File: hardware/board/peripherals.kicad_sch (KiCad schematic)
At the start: 6 parts, among them U1 RK3568, X1 24 MHz

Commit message: added stuff
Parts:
- added J1: Micro_SD_Card, symbol Connector:Micro_SD_Card
- C1, C2: value 10pF -> 10pF C0G; Class C0G -> (none)
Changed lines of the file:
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@@
 		(dnp no)
 		(property "Reference" "C1"
-			(at 185.42 139.7 0)
+			(at 185.928 140.208 0)
 			(effects
 				(font
@@
 			)
 		)
-		(property "Value" "10pF"
-			(at 185.42 142.24 0)
+		(property "Value" "10pF C0G"
+			(at 186.182 142.24 0)
 			(effects
 				(font
@@
 				)
 				(hide yes)
-			)
-		)
-		(property "Class" "C0G"
-			(at 187.452 144.526 0)
-			(effects
-				(font
-					(size 1.27 1.27)
-				)
 			)
 		)
@@
 			)
 		)
-		(property "Value" "10pF"
+		(property "Value" "10pF C0G"
 			(at 165.1 142.24 0)
 			(effects
@@
 			)
 		)
-		(property "Class" "C0G"
-			(at 163.068 144.526 0)
-			(effects
-				(font
-					(size 1.27 1.27)
-				)
-			)
-		)
 		(pin "2"
 		)
@@
 					(unit 1)
 				)
+			)
+		)
+	)
+	(symbol
+		(lib_id "Connector:Micro_SD_Card")
+		(at 217.17 54.61 0)
+		(unit 1)
+		(exclude_from_sim no)
+		(in_bom yes)
+		(on_board yes)
+		(dnp no)
+		(fields_autoplaced yes)
+		(property "Reference" "J1"
+			(at 217.805 35.56 0)
+			(effects
+				(font
+					(size 1.27 1.27)
+				)
+			)
+		)
+		(property "Value" "Micro_SD_Card"
+			(at 217.805 38.1 0)
+			(effects
+				(font
+					(size 1.27 1.27)
+				)
+			)
+		)
+		(property "Footprint" ""
+			(at 246.38 46.99 0)
+			(effects
+				(font
+					(size 1.27 1.27)
+				)
+				(hide yes)
+			)
+		)
+		(property "Datasheet" "https://www.we-online.com/components/products/datasheet/693072010801.pdf"
+			(at 217.17 54.61 0)
+			(effects
+				(font
+					(size 1.27 1.27)
+				)
+				(hide yes)
+			)
+		)
+		(property "Description" "Micro SD Card Socket"
+			(at 217.17 54.61 0)
+			(effects
+				(font
+					(size 1.27 1.27)
+				)
+				(hide yes)
+			)
+		)
+		(pin "6"
+		)
+		(pin "9"
+		)
+		(pin "3"
+		)
+		(pin "8"
+		)
+		(pin "1"
+		)
+		(pin "4"
+		)
+		(pin "2"
+		)
+		(pin "5"
+		)
+		(pin "7"
+		)
+		(instances
+			(project ""
+				(path "/3bc38516-4fe0-4022-adb8-9fd55b66cd2d/dbcf2505-8053-4a61-9f30-22e0e1eb9f47"
+					(reference "J1")
+					(unit 1)
+				)

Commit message: emmc stuff
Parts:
- U1: LCSC (none) -> C3345225
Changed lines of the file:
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@@
+			)
+		)
+		(property "LCSC" "C3345225"
+			(at 81.28 82.55 0)
+			(effects
+				(font
+					(size 1.27 1.27)
+				)
+				(hide yes)
 			)
 		)

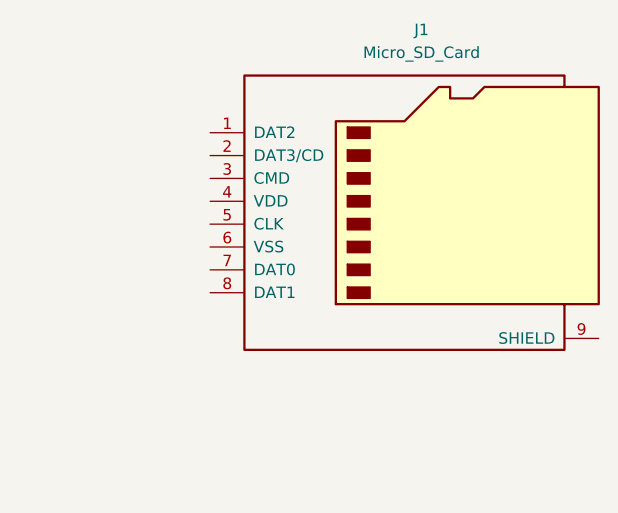
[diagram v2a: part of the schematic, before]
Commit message: MIPI IS FAKE
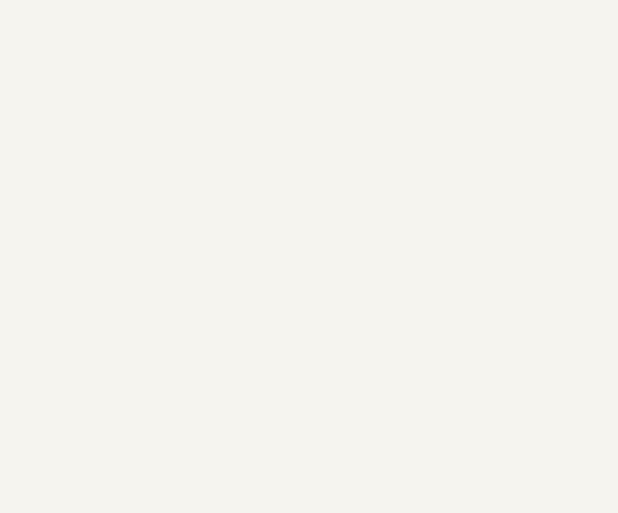
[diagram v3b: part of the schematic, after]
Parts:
- removed J1: Micro_SD_Card, symbol Connector:Micro_SD_Card
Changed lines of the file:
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@@
-		)
-	)
-	(symbol
-		(lib_id "Connector:Micro_SD_Card")
-		(at 217.17 54.61 0)
-		(unit 1)
-		(exclude_from_sim no)
-		(in_bom yes)
-		(on_board yes)
-		(dnp no)
-		(fields_autoplaced yes)
-		(property "Reference" "J1"
-			(at 217.805 35.56 0)
-			(effects
-				(font
-					(size 1.27 1.27)
-				)
-			)
-		)
-		(property "Value" "Micro_SD_Card"
-			(at 217.805 38.1 0)
-			(effects
-				(font
-					(size 1.27 1.27)
-				)
-			)
-		)
-		(property "Footprint" ""
-			(at 246.38 46.99 0)
-			(effects
-				(font
-					(size 1.27 1.27)
-				)
-				(hide yes)
-			)
-		)
-		(property "Datasheet" "https://www.we-online.com/components/products/datasheet/693072010801.pdf"
-			(at 217.17 54.61 0)
-			(effects
-				(font
-					(size 1.27 1.27)
-				)
-				(hide yes)
-			)
-		)
-		(property "Description" "Micro SD Card Socket"
-			(at 217.17 54.61 0)
-			(effects
-				(font
-					(size 1.27 1.27)
-				)
-				(hide yes)
-			)
-		)
-		(pin "6"
-		)
-		(pin "9"
-		)
-		(pin "3"
-		)
-		(pin "8"
-		)
-		(pin "1"
-		)
-		(pin "4"
-		)
-		(pin "2"
-		)
-		(pin "5"
-		)
-		(pin "7"
-		)
-		(instances
-			(project ""
-				(path "/3bc38516-4fe0-4022-adb8-9fd55b66cd2d/dbcf2505-8053-4a61-9f30-22e0e1eb9f47"
-					(reference "J1")
-					(unit 1)
-				)
-			)
 		)
 	)

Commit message: aaa
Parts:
- added C198: 1uF X5R 10V, Capacitor_SMD:C_0402_1005Metric, symbol Device:C
- added C199: 10pF C0G 50V, Capacitor_SMD:C_0402_1005Metric, symbol Device:C
- added CN1: PJ-393 8PJ, lcsc:AUDIO-SMD_PJ-393-8PJ, symbol lcsc:PJ-3938PJ
- added R129: 100R 5%, Resistor_SMD:R_0402_1005Metric, symbol Device:R
- added R139: 2.2K 5%, Resistor_SMD:R_0402_1005Metric, symbol Device:R
- added R140, R141: 0R 5%, Resistor_SMD:R_0402_1005Metric, symbol Device:R
- added U46, U48: ESD5451N_C5261080, lcsc:DFN1006-2L-BI, symbol lcsc:ESD5451N_C5261080
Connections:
- net GND: now also C198.2, C199.2, U46.1, U48.1
- new net: CN1.1, CN1.5, R140.1, U48.2
- new net: C198.1, R129.1, R139.2
- new net: CN1.2, CN1.6, R141.1
- new net: CN1.3, CN1.7
- new net: CN1.4, CN1.8
- new net HPL_OUT: R140.2
- new net HPR_OUT: R141.2
- new net MIC1_INP: C199.1, R139.1, U46.2
- new net VCCIO_ACODEC: R129.2

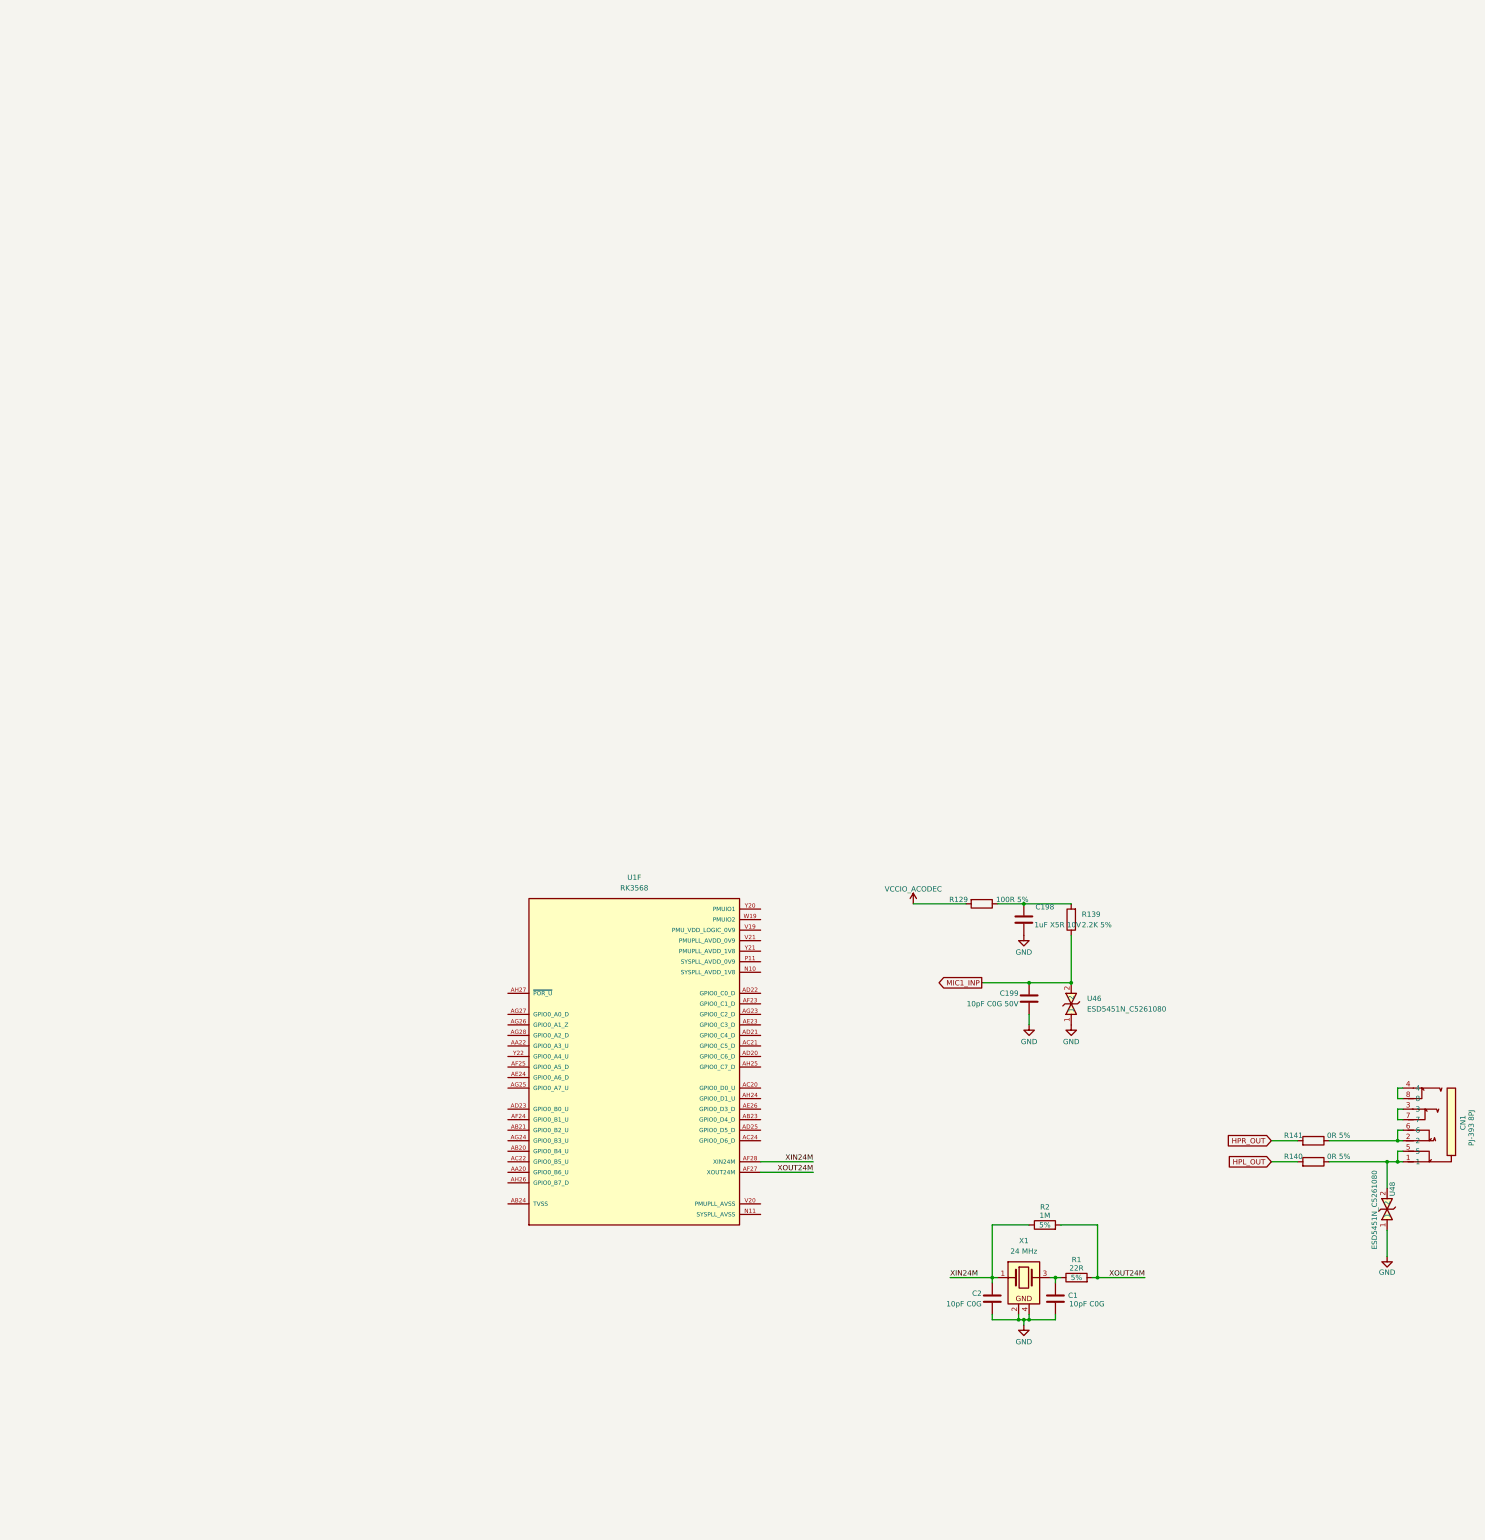
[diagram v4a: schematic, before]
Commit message: add in pcie and ddr4
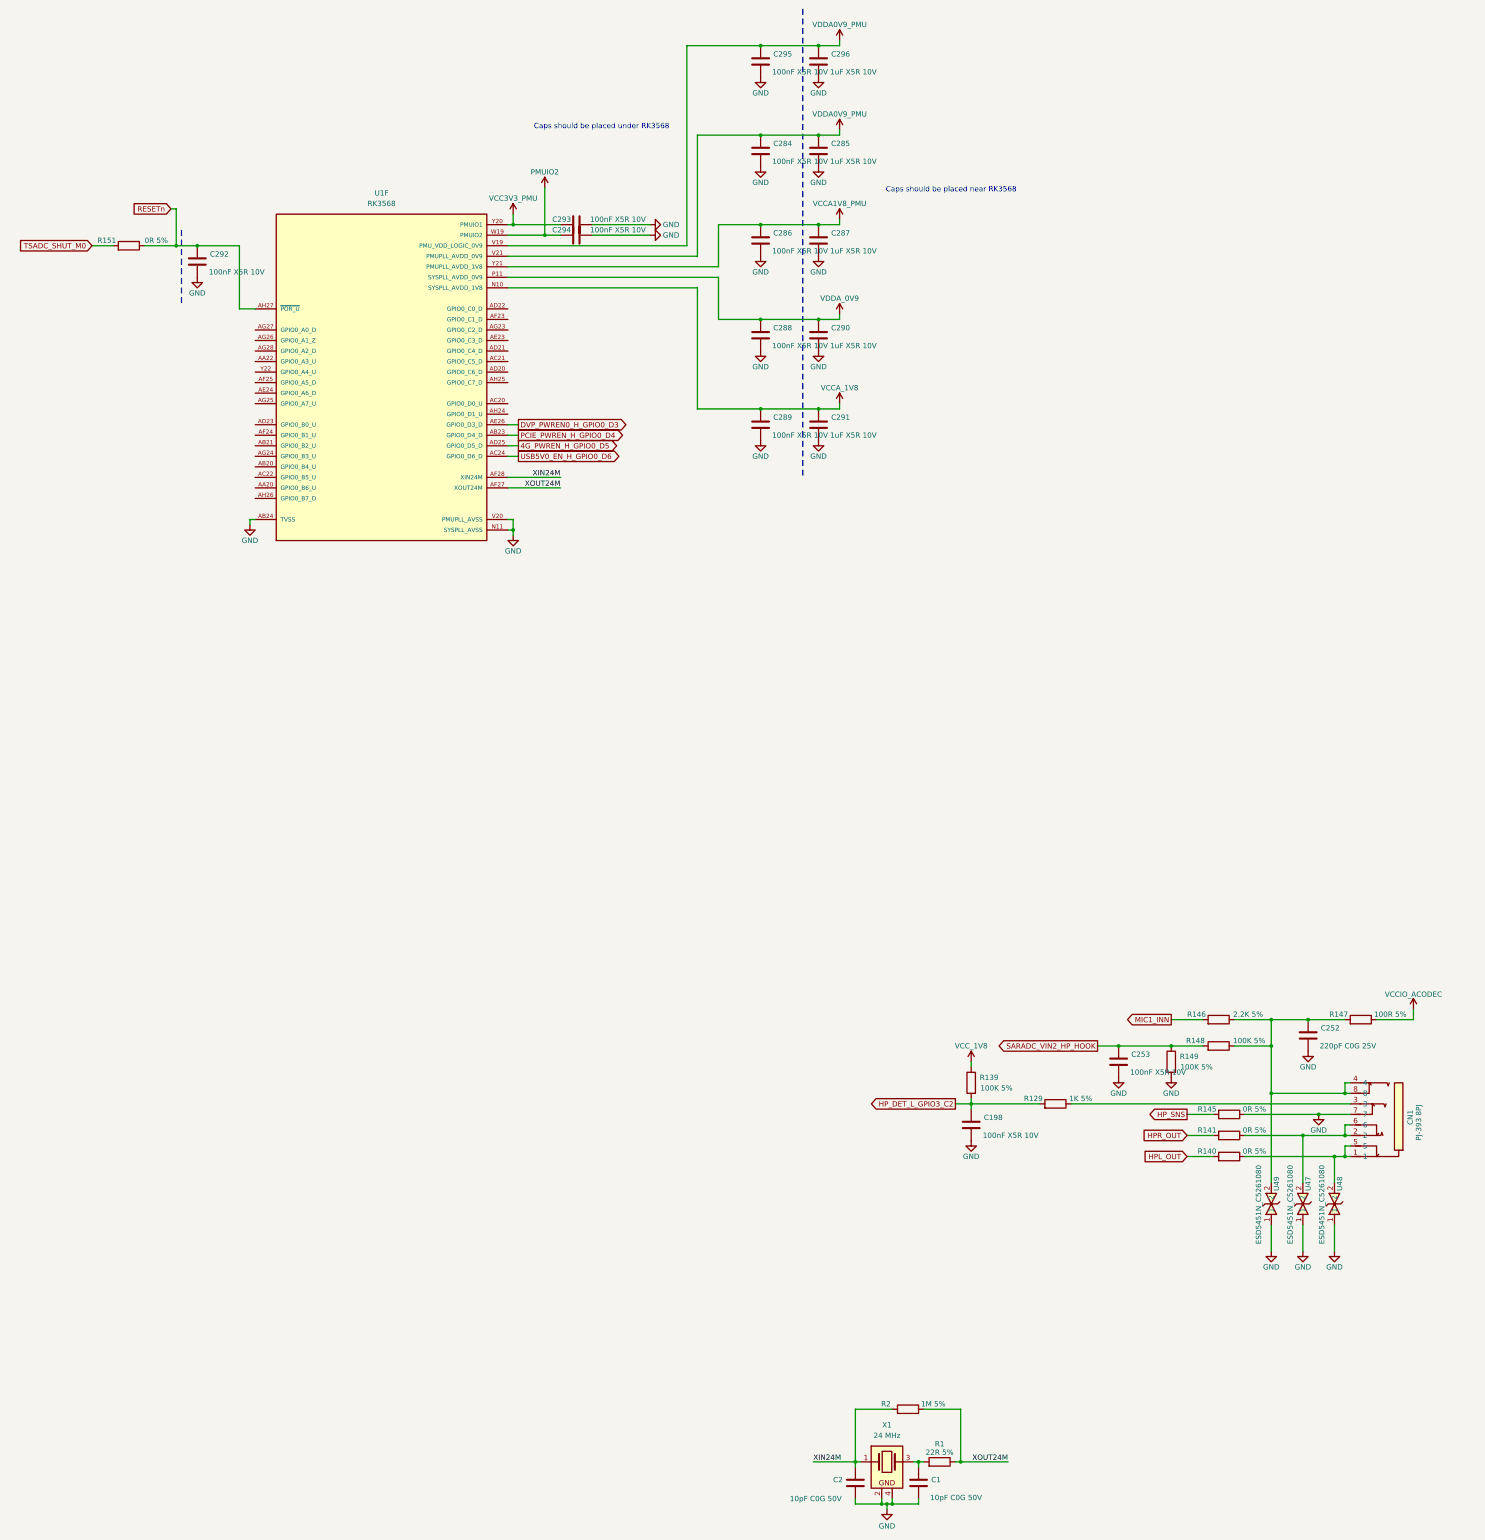
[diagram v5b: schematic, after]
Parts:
- removed C199: 10pF C0G 50V, Capacitor_SMD:C_0402_1005Metric, symbol Device:C
- removed U46: ESD5451N_C5261080, lcsc:DFN1006-2L-BI, symbol lcsc:ESD5451N_C5261080
- added C252: 220pF C0G 25V, Capacitor_SMD:C_0402_1005Metric, symbol Device:C
- added C253: 100nF X5R 10V, Capacitor_SMD:C_0402_1005Metric, symbol Device:C
- added C284, C286, C288, C289, C292, C293, C294, C295: 100nF X5R 10V, Capacitor_SMD:C_0201_0603Metric, symbol Device:C
- added C285, C287, C290, C291, C296: 1uF X5R 10V, Capacitor_SMD:C_0402_1005Metric, symbol Device:C
- added R145, R151: 0R 5%, Resistor_SMD:R_0402_1005Metric, symbol Device:R
- added R146: 2.2K 5%, Resistor_SMD:R_0402_1005Metric, symbol Device:R
- added R147: 100R 5%, Resistor_SMD:R_0402_1005Metric, symbol Device:R
- added R148, R149: 100K 5%, Resistor_SMD:R_0402_1005Metric, symbol Device:R
- added U47, U49: ESD5451N_C5261080, lcsc:DFN1006-2L-BI, symbol lcsc:ESD5451N_C5261080
- C1, C2: value 10pF C0G -> 10pF C0G 50V
- C198: value 1uF X5R 10V -> 100nF X5R 10V
- R1: value 22R -> 22R 5%; Tolerance 5% -> (none)
- R129: value 100R 5% -> 1K 5%
- R139: value 2.2K 5% -> 100K 5%
- R2: value 1M -> 1M 5%; Tolerance 5% -> (none)
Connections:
- net GND: now also CN1.7, U1.AB24 (TVSS), U1.N11 (SYSPLL_AVSS), U1.V20 (PMUPLL_AVSS), C252.2, C253.2, C284.2, C285.2, C286.2, C287.2, C288.2, C289.2, C290.2, C291.2, C292.2, C293.2, C294.2, C295.2, C296.2, R145.1, R149.2, U47.1, U49.1
- net VCCIO_ACODEC: now also R147.1; no longer R129.2
- net XIN24M: now also R2.2; no longer R2.1
- net XOUT24M: now also R1.1, R2.1; no longer R1.2, R2.2
- net PCIE_PWREN_H_GPIO0_D4: now reaches U1.AB23 (GPIO0_D4_D)
- net USB5V0_EN_H_GPIO0_D6: now reaches U1.AC24 (GPIO0_D6_D)
- net 4G_PWREN_H_GPIO0_D5: now reaches U1.AD25 (GPIO0_D5_D)
- net DVP_PWREN0_H_GPIO0_D3: now reaches U1.AE26 (GPIO0_D3_D)
- net RESETn: now reaches U1.AH27 (~{POR_U})
- net RESETn: now also C292.1, R151.1
- net VCCA_1V8: now reaches U1.N10 (SYSPLL_AVDD_1V8)
- net VCCA_1V8: now also C289.1, C291.1
- net VDDA_0V9: now reaches U1.P11 (SYSPLL_AVDD_0V9)
- net VDDA_0V9: now also C288.1, C290.1
- net VDDA0V9_PMU: now reaches U1.V19 (PMU_VDD_LOGIC_0V9)
- net VDDA0V9_PMU: now also U1.V21 (PMUPLL_AVDD_0V9), C284.1, C285.1, C295.1, C296.1
- net PMUIO2: now reaches U1.W19 (PMUIO2)
- net PMUIO2: now also C294.1
- net VCC3V3_PMU: now reaches U1.Y20 (PMUIO1)
- net VCC3V3_PMU: now also C293.1
- net VCCA1V8_PMU: now reaches U1.Y21 (PMUPLL_AVDD_1V8)
- net VCCA1V8_PMU: now also C286.1, C287.1
- net HP_DET_L_GPIO3_C2: now reaches C198.1, R139.2
- net HP_DET_L_GPIO3_C2: now also R129.2; no longer R129.1
- net at C1.1, X1.3: now also R1.2; no longer R1.1
- net at CN1.2, CN1.6, R141.1: now also U47.2
- net at CN1.3: now also R129.1; no longer CN1.7
- net at CN1.4, CN1.8: now also C252.1, R146.1, R147.2, R148.1, U49.2
- net MIC1_INP renamed VCC_1V8
- new net HP_SNS: R145.2
- new net MIC1_INN: R146.2
- new net SARADC_VIN2_HP_HOOK: C253.1, R148.2, R149.1
- new net TSADC_SHUT_M0: R151.2
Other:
- note added: "Caps should be placed near RK3568"
- note added: "Caps should be placed under RK3568"
- moved on the sheet: C1, CN1, R140, R141, U1F, U48, X1

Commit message: finished schematic!
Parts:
- added C353, C354, C355, C356, C357: 1nF X5R 10V, Capacitor_SMD:C_0402_1005Metric, symbol Device:C
- added C358, C359: 100nF X5R 10V, Capacitor_SMD:C_0201_0603Metric, symbol Device:C
- added J4: Conn_01x04, Connector_PinHeader_2.54mm:PinHeader_1x04_P2.54mm_Vertical, symbol Connector_Generic:Conn_01x04
- added R180, R181, R183, R184, R185: 100R 5%, Resistor_SMD:R_0402_1005Metric, symbol Device:R
- added R182: 120R 5%, Resistor_SMD:R_0402_1005Metric, symbol Device:R
- added R186, R187, R188, R189: 10K 1%, Resistor_SMD:R_0402_1005Metric, symbol Device:R
- added R193, R194: 2.2K 5%, Resistor_SMD:R_0402_1005Metric, symbol Device:R
- added R198, R199: 10K 5%, Resistor_SMD:R_0402_1005Metric, symbol Device:R
- added SW1, SW2, SW3: TS24CA, lcsc:SW-SMD_2P-TS24CA, symbol lcsc:TS24CA
- added TP10, TP11: TestPoint, TestPoint:TestPoint_Pad_D1.0mm, symbol Connector:TestPoint
- added unit 14 of U1
- added U58, U59, U60, U61, U62: ESD5451N_C5261080, lcsc:DFN1006-2L-BI, symbol lcsc:ESD5451N_C5261080
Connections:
- net GND: now also C353.2, C354.2, C355.2, C356.2, C357.2, C358.2, C359.2, J4.4 (Pin_4), R182.2, R187.2, R189.2, SW1.1, SW2.1, SW3.1, TP11.1, U58.2, U59.2, U60.2, U61.2, U62.2
- net PMUIO2: now also J4.1 (Pin_1), R193.1, R194.1
- net RESETn: now also R184.2
- net SARADC_VIN2_HP_HOOK: now also C355.1, U1.D24 (SARADC_VIN2)
- net TSADC_SHUT_M0: now also U1.AG26 (GPIO0_A1_Z)
- net VCCA_1V8: now also C359.1, R198.2, R199.2, U1.H22 (SARADC_AVDD_1V8)
- net VCC_1V8: now also C358.1, R186.1, R188.1, U1.H20 (OTP_VCC18)
- net PMIC_INT_L: now reaches U1.AA22 (GPIO0_A3_U)
- net I2C0_SDA_PMIC: now reaches U1.AB21 (GPIO0_B2_U)
- net I2C0_SDA_PMIC: now also R194.2
- net UART2_RX_M0_DEBUG: now reaches U1.AC20 (GPIO0_D0_U)
- net UART2_RX_M0_DEBUG: now also R180.2, R182.1
- net USBCC_INT_L_GPIO0_C5: now reaches U1.AC21 (GPIO0_C5_D)
- net HALL_INT_L_GPIO0_C6: now reaches U1.AD20 (GPIO0_C6_D)
- net WIFI_WAKE_HOST_H_GPIO0_C4: now reaches U1.AD21 (GPIO0_C4_D)
- net WIFI_REG_ON_H_GPIO0_C0: now reaches U1.AD22 (GPIO0_C0_D)
- net HOST_WAKE_BT_H_GPIO0_B0: now reaches U1.AD23 (GPIO0_B0_U)
- net LCD0_BL_PWM4: now reaches U1.AE23 (GPIO0_C3_D)
- net USB_HOST_PWREN_H_GPIO0_A6: now reaches U1.AE24 (GPIO0_A6_D)
- net BT_REG_ON_H_GPIO0_C1: now reaches U1.AF23 (GPIO0_C1_D)
- net I2C0_SCL_PMIC: now reaches U1.AF24 (GPIO0_B1_U)
- net I2C0_SCL_PMIC: now also R193.2
- net SDMMC0_PWREN_L: now reaches U1.AF25 (GPIO0_A5_D)
- net CHG_INT_L_GPIO0_C2: now reaches U1.AG23 (GPIO0_C2_D)
- net FLASH_VOL_SEL: now reaches U1.AG25 (GPIO0_A7_U)
- net WIFI_PWREN_GPIO0_A0: now reaches U1.AG27 (GPIO0_A0_D)
- net PMIC_SLEEP_H: now reaches U1.AG28 (GPIO0_A2_D)
- net UART2_TX_M0_DEBUG: now reaches U1.AH24 (GPIO0_D1_U)
- net UART2_TX_M0_DEBUG: now also R181.2
- net LCD0_PWREN_H_GPIO0_C7: now reaches U1.AH25 (GPIO0_C7_D)
- net BT_WAKE_HOST_H_GPIO0_B7: now reaches U1.AH26 (GPIO0_B7_D)
- net SDMMC0_DET_L: now reaches U1.Y22 (GPIO0_A4_U)
- net 4G_PWREN_H_GPIO0_D5: no longer names the net of U1.AD25 (GPIO0_D5_D)
- new net: R184.1, SW2.2, U61.1
- new net: R185.1, SW3.2
- new net: R183.1, SW1.2, U60.1
- new net: J4.2 (Pin_2), R180.1, U59.1
- new net: J4.3 (Pin_3), R181.1, U58.1
- new net BATT_TC_L: C357.1, R198.1, U1.G21 (SARADC_VIN4)
- new net PMIC_PWRON: R183.2
- new net SARADC_VIN0_KEY/RECOVERY: C353.1, R185.2, R199.1, TP10.1, U1.B27 (SARADC_VIN0), U62.1
- new net SARADC_VIN1_HW_ID: C354.1, R186.2, R187.1, U1.C26 (SARADC_VIN1)
- new net SARADC_VIN3_BOM_ID: C356.1, R188.2, R189.1, U1.E23 (SARADC_VIN3)
- no-connect marks 0 -> 14
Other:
- note added: "Crystal"
- note added: "Debug UART"
- note added: "HW / BOM ID"
- note added: "Headphone Jack"
- note added: "I2C1"
- note added: "If SARADC_VIN0=0V at after power on and reset, then system will enter into loader mode."
- note added: "Power On"
- note added: "Recovery"
- note added: "Reset"
- note added: "Stuff for 1.8V, empty for 3.3V"
- moved on the sheet: C1, C198, C2, C252, C253, C284, C285, C286, C287, C288, C289, C290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

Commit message: finished beautifying schematic
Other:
- note added: "Frost"
- note added: "RK3568"
- note removed: "Caps should be placed near RK3568"
- moved on the sheet: C1, C198, C2, C252, C253, C284, C285, C286, C287, C288, C289, C290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
